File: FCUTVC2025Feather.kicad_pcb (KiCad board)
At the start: 2 copper layers, 60 x 131.5 mm, 53 parts, among them J1 Micro_SD_Card_Det2, J10 Conn_01x04, J11 Conn_01x04, J12 Conn_01x05, J13 Conn_01x05, J2 Conn_01x03, J3 Conn_01x03, J4 Conn_01x02, J5 Conn_01x02, J6 Conn_01x02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

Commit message: fixed drc
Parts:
- moved C30 0.20 mm to (131.2, 49.0)
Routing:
- net /MISO: track 50.2 -> 64.1 mm, vias 2 -> 3
- net +5V: track 81.2 -> 82.2 mm
- net /SCK: track 59.1 -> 58.5 mm, vias 5 -> 4
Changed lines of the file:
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@@
 	(footprint "Capacitor_SMD:C_0402_1005Metric"
 		(layer "B.Cu")
-		(at 131.2 48.8)
+		(at 131.2 49)
 		(descr "Capacitor SMD 0402 (1005 Metric), square (rectangular) end terminal, IPC_7351 nominal, (Body size source: IPC-SM-782 page 76, https://www.pcb-3d.com/wordpress/wp-content/uploads/ipc-sm-782a_amendment_1_and_2.pdf), generated with kicad-footprint-generator")
 		(tags "capacitor")
@@
 		)
 		(fp_line
-			(start -0.508 -2.8194)
-			(end -0.508 -2.7559)
-			(stroke
-				(width 0.1524)
-				(type solid)
-			)
-			(layer "B.CrtYd")
-		)
-		(fp_line
 			(start -0.508 -2.7559)
 			(end -2.4892 -2.7559)
@@
 		)
 		(fp_line
-			(start -0.508 2.7559)
-			(end -0.508 2.8194)
-			(stroke
-				(width 0.1524)
-				(type solid)
-			)
-			(layer "B.CrtYd")
-		)
-		(fp_line
-			(start -0.508 2.8194)
-			(end 0.508 2.8194)
-			(stroke
-				(width 0.1524)
-				(type solid)
-			)
-			(layer "B.CrtYd")
-		)
-		(fp_line
-			(start 0.508 -2.8194)
-			(end -0.508 -2.8194)
-			(stroke
-				(width 0.1524)
-				(type solid)
-			)
-			(layer "B.CrtYd")
-		)
-		(fp_line
-			(start 0.508 -2.7559)
-			(end 0.508 -2.8194)
-			(stroke
-				(width 0.1524)
-				(type solid)
-			)
-			(layer "B.CrtYd")
-		)
-		(fp_line
-			(start 0.508 2.8194)
-			(end 0.508 2.7559)
-			(stroke
-				(width 0.1524)
-				(type solid)
-			)
-			(layer "B.CrtYd")
-		)
-		(fp_line
-			(start 2.413508 -2.7204)
-			(end 2.4892 -2.723339)
-			(stroke
-				(width 0.1524)
-				(type solid)
-			)
-			(layer "B.CrtYd")
-		)
-		(fp_line
-			(start 2.4892 -2.7559)
-			(end 0.508 -2.7559)
+			(start -0.508 -2.7559)
+			(end 3.327908 -2.7559)
 			(stroke
 				(width 0.1524)
-				(type solid)
+				(type default)
 			)
 			(layer "B.CrtYd")
 		)
 		(fp_line
-			(start 2.4892 -2.723339)
-			(end 2.4892 -2.7559)
+			(start -0.508 2.7559)
+			(end 3.327908 2.7152)
 			(stroke
 				(width 0.1524)
-				(type solid)
+				(type default)
 			)
 			(layer "B.CrtYd")
@@
 	)
 	(via
-		(at 122.2 54.9)
+		(at 122.1 54.887952)
 		(size 0.6)
 		(drill 0.3)
@@
 	)
 	(via
-		(at 130.6 48.1)
+		(at 130.6 48.2)
 		(size 0.6)
 		(drill 0.3)
@@
 	)
 	(segment
+		(start 132.7 54.9)
+		(end 132.3 54.9)
+		(width 0.2)
+		(layer "F.Cu")
+		(net 5)
+	)
+	(segment
 		(start 123.2 59.8)
 		(end 123 60)
@@
 		(net 5)
 	)
+	(segment
+		(start 132.3 54.9)
+		(end 130.200555 56.999445)
+		(width 0.2)
+		(layer "F.Cu")
+		(net 5)
+	)
+	(segment
+		(start 130.200555 56.999445)
+		(end 124.074445 56.999445)
+		(width 0.2)
+		(layer "F.Cu")
+		(net 5)
+	)
+	(segment
+		(start 124.074445 56.999445)
+		(end 123.7 56.625)
+		(width 0.2)
+		(layer "F.Cu")
+		(net 5)
+	)
+	(via
+		(at 132.7 54.9)
+		(size 0.6)
+		(drill 0.3)
+		(layers "F.Cu" "B.Cu")
+		(net 5)
+	)
 	(via
 		(at 123.7 56.625)
@@
 	)
 	(segment
+		(start 133.01 54.59)
+		(end 133.01 51.1)
+		(width 0.2)
+		(layer "B.Cu")
+		(net 5)
+	)
+	(segment
 		(start 118.361865 58.6)
 		(end 117.2475 59.714365)
@@
 	)
 	(segment
+		(start 132.7 54.9)
+		(end 133.01 54.59)
+		(width 0.2)
+		(layer "B.Cu")
+		(net 5)
+	)
+	(segment
 		(start 133.975 59)
 		(end 123.045 69.93)
@@
 	)
 	(segment
+		(start 139.2675 39.3675)
+		(end 139.2675 49.61)
+		(width 0.4)
+		(layer "B.Cu")
+		(net 19)
+	)
+	(segment
+		(start 113 46.2)
+		(end 115.25 43.95)
+		(width 0.4)
+		(layer "B.Cu")
+		(net 19)
+	)
+	(segment
 		(start 102.75 66.675)
 		(end 101.75 66.675)
@@
 	)
 	(segment
-		(start 139.2675 41.061078)
-		(end 139.2675 49.61)
-		(width 0.4)
+		(start 101.75 66.675)
+		(end 101.65 66.575)
+		(width 0.2)
 		(layer "B.Cu")
 		(net 19)
 	)
 	(segment
-		(start 101.75 66.675)
-		(end 101.65 66.575)
-		(width 0.2)
+		(start 115.25 43.95)
+		(end 115.25 38.75)
+		(width 0.4)
 		(layer "B.Cu")
 		(net 19)
@@
 	)
 	(segment
-		(start 115.25 38.75)
-		(end 116.25 37.75)
-		(width 0.4)
-		(layer "B.Cu")
-		(net 19)
-	)
-	(segment
-		(start 135.956422 37.75)
-		(end 139.2675 41.061078)
-		(width 0.4)
-		(layer "B.Cu")
-		(net 19)
-	)
-	(segment
-		(start 116.25 37.75)
-		(end 135.956422 37.75)
+		(start 137.65 37.75)
+		(end 139.2675 39.3675)
 		(width 0.4)
 		(layer "B.Cu")
@@
 	)
 	(segment
-		(start 115.25 43.95)
-		(end 115.25 38.75)
-		(width 0.4)
-		(layer "B.Cu")
-		(net 19)
-	)
-	(segment
-		(start 113 46.2)
-		(end 115.25 43.95)
+		(start 115.25 38.75)
+		(end 116.25 37.75)
 		(width 0.4)
 		(layer "B.Cu")
@@
 	)
 	(segment
+		(start 116.25 37.75)
+		(end 137.65 37.75)
+		(width 0.4)
+		(layer "B.Cu")
+		(net 19)
+	)
+	(segment
 		(start 140.95 133.7)
 		(end 140.95 133.63)
@@
 	)
 	(segment
-		(start 121.7 57.6)
-		(end 121.7 54.9025)
+		(start 121.5 57.4)
+		(end 121.5 54.7025)
 		(width 0.2)
 		(layer "B.Cu")
@@
 	(segment
 		(start 121.975 57.875)
-		(end 121.7 57.6)
+		(end 121.5 57.4)
 		(width 0.2)
 		(layer "B.Cu")
@@
 	)
 	(segment
-		(start 127.075 57.875)
-		(end 124.925 57.875)
+		(start 121.5 54.7025)
+		(end 118.9475 52.15)
 		(width 0.2)
 		(layer "B.Cu")
@@
 	)
 	(segment
-		(start 121.7 54.9025)
-		(end 118.9475 52.15)
+		(start 127.075 57.875)
+		(end 124.925 57.875)
 		(width 0.2)
 		(layer "B.Cu")
@@
 	)
 	(via
-		(at 123 55)
-		(size 0.6)
-		(drill 0.3)
-		(layers "F.Cu" "B.Cu")
-		(net 27)
-	)
-	(via
 		(at 127 52)
 		(size 0.6)
@@
 	)
 	(segment
-		(start 123.875 54.125)
-		(end 123 55)
+		(start 115.8 53.541865)
+		(end 118.341865 51)
 		(width 0.2)
 		(layer "B.Cu")
@@
 	)
 	(segment
-		(start 131.51 49.5)
-		(end 131.155 49.145)
+		(start 132.429179 50.255692)
+		(end 132.429179 48.714179)
 		(width 0.2)
 		(layer "B.Cu")
@@
 	)
 	(segment
-		(start 124.925 54.125)
-		(end 124.925 54.075)
+		(start 120.75 51)
+		(end 123.875 54.125)
 		(width 0.2)
 		(layer "B.Cu")
@@
 	)
 	(segment
-		(start 116.5 65.1)
-		(end 115.8 64.4)
+		(start 123.875 54.125)
+		(end 124.925 54.125)
 		(width 0.2)
 		(layer "B.Cu")
@@
 	)
 	(segment
-		(start 120.203135 51.05)
-		(end 123 53.846865)
+		(start 131.155 47.44)
+		(end 131.155 47.09)
 		(width 0.2)
 		(layer "B.Cu")
@@
 	)
 	(segment
-		(start 123.475432 65.2)
-		(end 126 62.675432)
+		(start 124.925 54.125)
+		(end 124.925 54.075)
 		(width 0.2)
 		(layer "B.Cu")
@@
 	)
 	(segment
-		(start 131.51 49.9)
-		(end 131.51 49.5)
+		(start 116.5 65.1)
+		(end 115.8 64.4)
 		(width 0.2)
 		(layer "B.Cu")
@@
 	)
 	(segment
-		(start 123 53.846865)
-		(end 123 55)
+		(start 123.475432 65.2)
+		(end 126 62.675432)
 		(width 0.2)
 		(layer "B.Cu")
@@
 	)
 	(segment
-		(start 118.291865 51.05)
-		(end 120.203135 51.05)
-		(width 0.2)
-		(layer "B.Cu")
-		(net 27)
-	)
-	(segment
 		(start 126 62.675432)
 		(end 126 62.33)
@@
 	)
 	(segment
-		(start 115.8 64.4)
-		(end 115.8 53.541865)
+		(start 118.341865 51)
+		(end 120.75 51)
 		(width 0.2)
 		(layer "B.Cu")
@@
 	)
 	(segment
-		(start 124.925 54.125)
-		(end 123.875 54.125)
-		(width 0.2)
-		(layer "B.Cu")
-		(net 27)
-	)
-	(segment
 		(start 132.073487 49.9)
 		(end 132.429179 50.255692)
@@
 	)
 	(segment
-		(start 131.155 47.09)
-		(end 131.155 49.145)
+		(start 131.51 49.9)
+		(end 132.073487 49.9)
 		(width 0.2)
 		(layer "B.Cu")
@@
 	)
 	(segment
-		(start 131.51 49.9)
-		(end 132.073487 49.9)
+		(start 132.429179 48.714179)
+		(end 131.155 47.44)
 		(width 0.2)
 		(layer "B.Cu")
@@
 	)
 	(segment
-		(start 115.8 53.541865)
-		(end 118.291865 51.05)
+		(start 115.8 64.4)
+		(end 115.8 53.541865)
 		(width 0.2)
 		(layer "B.Cu")

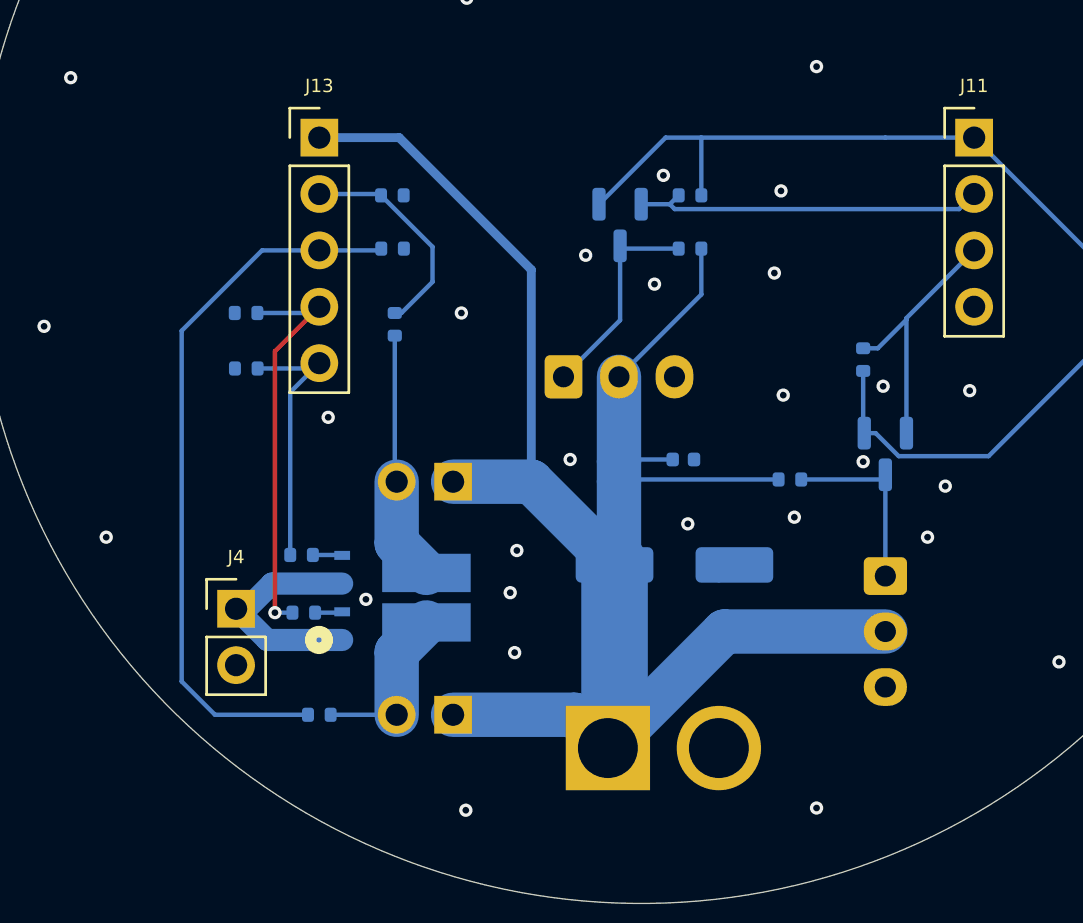
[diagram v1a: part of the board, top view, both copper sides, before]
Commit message: changed servo and pyro headers to JST XH (w/ hole). V1 complete
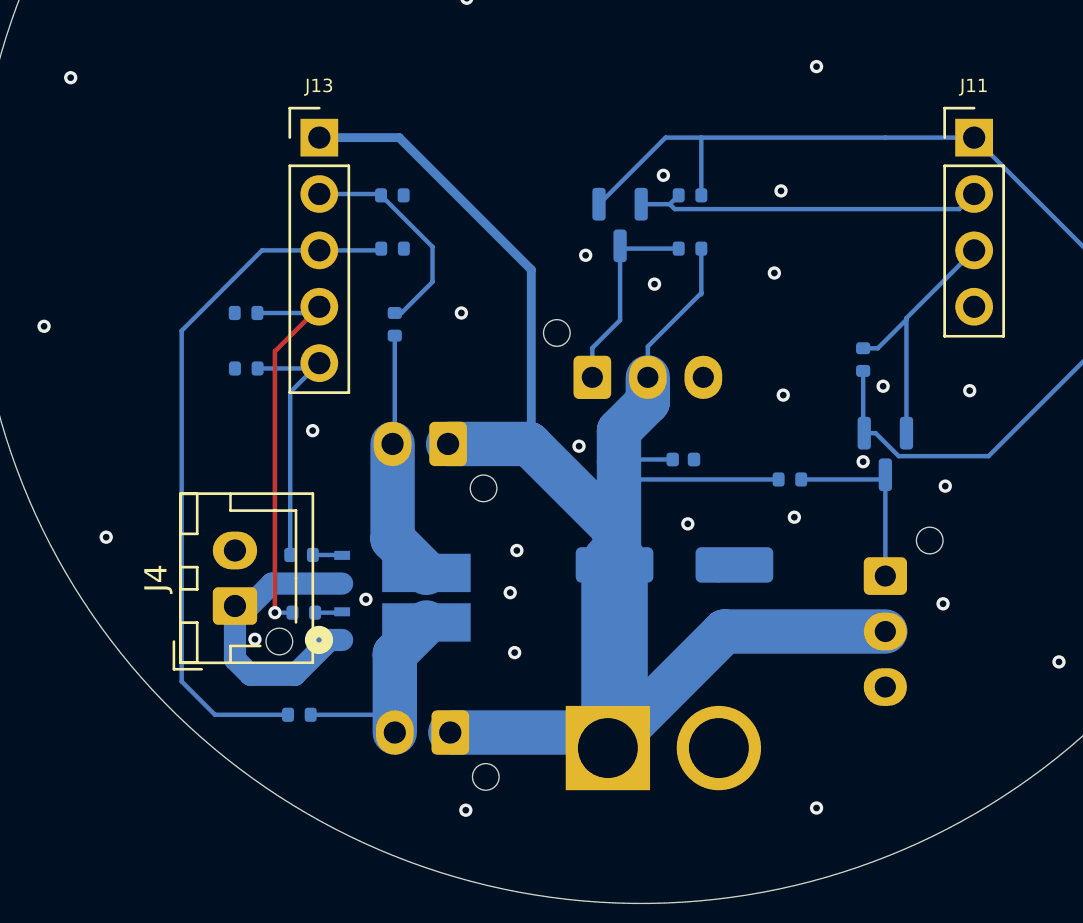
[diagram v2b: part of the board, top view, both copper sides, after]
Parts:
- J2, J3: footprint Connector_JST:JST_XH_B3B-XH-A_1x03_P2.50mm_Vertical -> Connector_JST:JST_XH_B3B-XH-AM_1x03_P2.50mm_Vertical
- J4, J6, J8: footprint Connector_PinHeader_2.54mm:PinHeader_1x02_P2.54mm_Vertical -> Connector_JST:JST_XH_B2B-XH-AM_1x02_P2.50mm_Vertical
- moved J8 1.71 mm to (120.3, 139.3), turned to 180 degrees
- moved J2 1.30 mm to (126.8, 136.3)
- moved R16 0.90 mm to (113.6, 151.5)
- moved J6 0.81 mm to (120.4, 152.3), turned to 180 degrees
- moved J4 0.13 mm to (110.7, 146.6), turned to 90 degrees
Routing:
- net Net-(J4-Pin_1): track 10.6 -> 13.4 mm
- net /PYO1: track 7.69 -> 9.42 mm
- net +6V/+8V: track 86.2 -> 87.2 mm
- net /PYC1: track 32.6 -> 31.7 mm
- net /SRV1O: track 9.65 -> 9.13 mm
- net GND: vias 98 -> 99

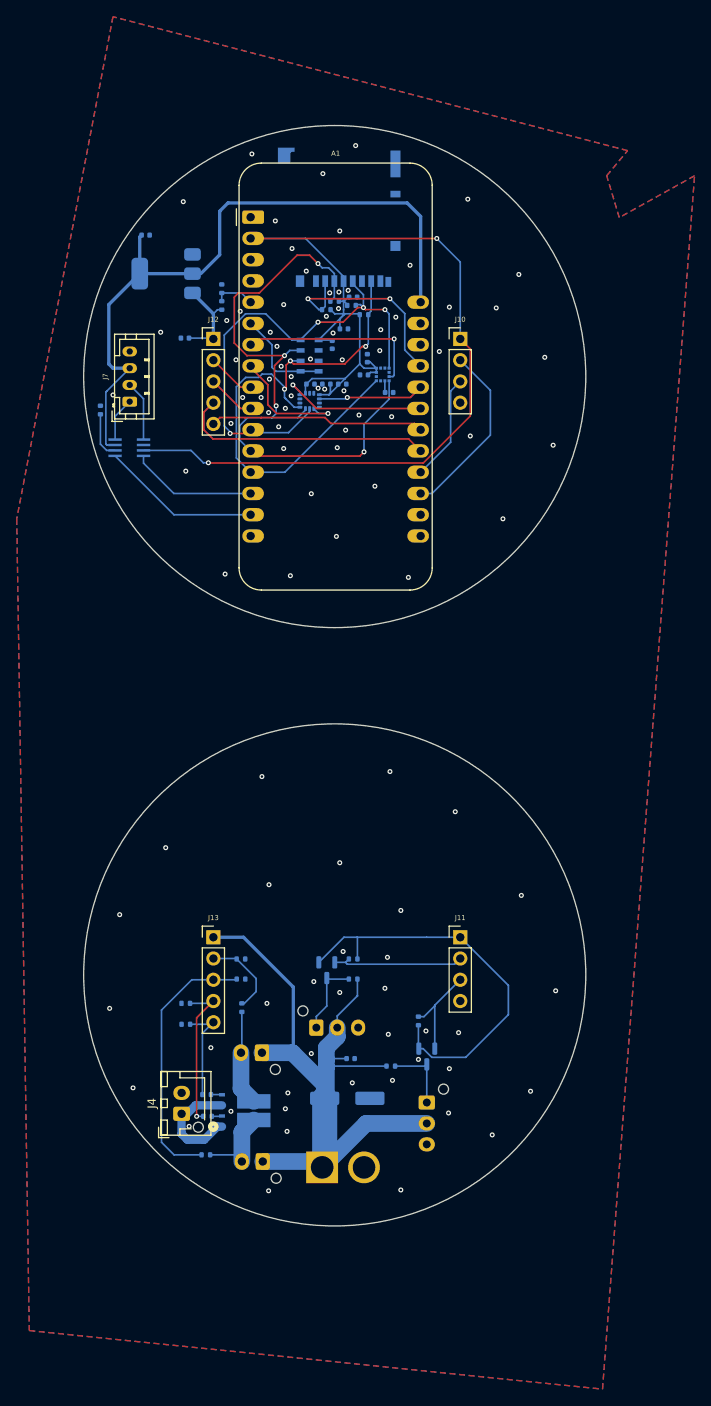
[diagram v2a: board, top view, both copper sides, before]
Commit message: added mounting holes (25mm 0 degrees, 150 degrees, 210 degrees)
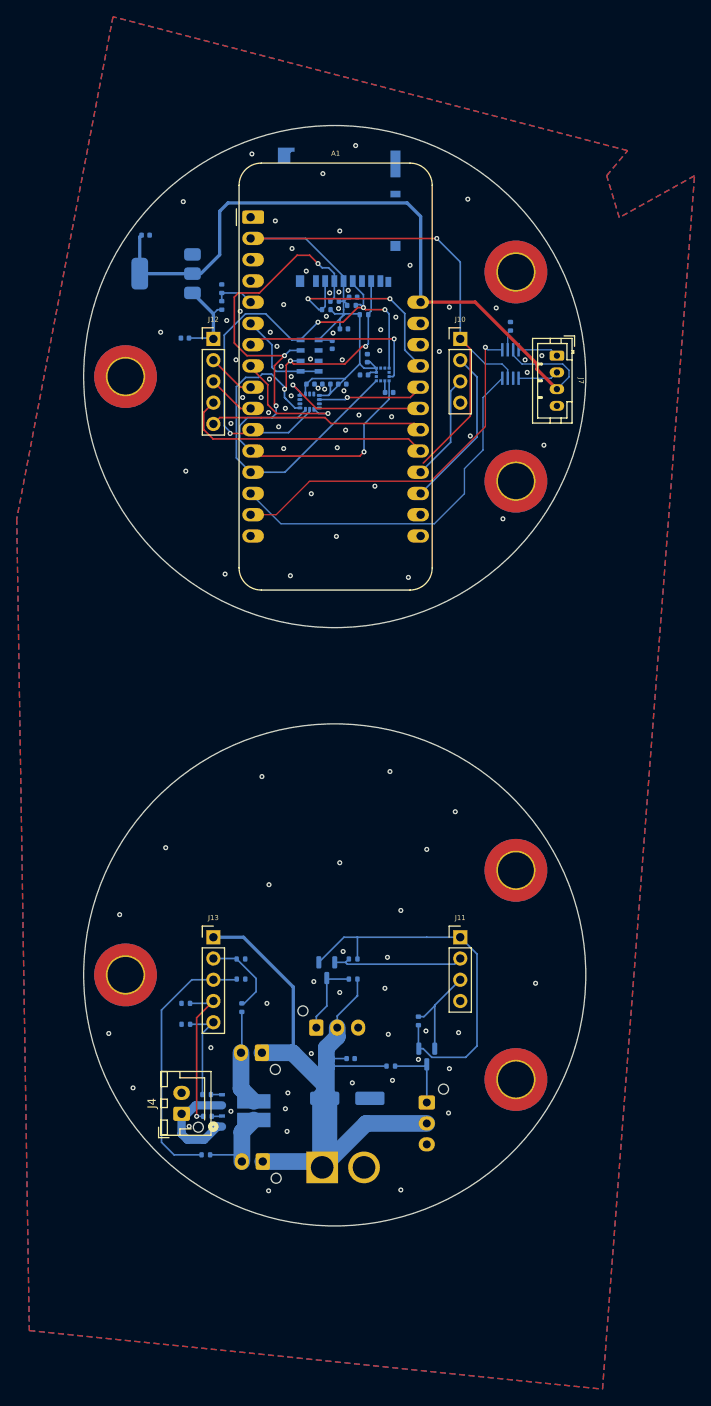
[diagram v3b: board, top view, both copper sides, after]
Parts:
- added H1: MountingHole_Pad, MountingHole:MountingHole_4.3mm_M4_DIN965_Pad_TopBottom, F.Cu at (104.0, 58.5)
- added H2: MountingHole_Pad, MountingHole:MountingHole_4.3mm_M4_DIN965_Pad_TopBottom, F.Cu at (150.7, 71.0)
- added H3: MountingHole_Pad, MountingHole:MountingHole_4.3mm_M4_DIN965_Pad_TopBottom, F.Cu at (150.7, 46.0)
- added H4: MountingHole_Pad, MountingHole:MountingHole_4.3mm_M4_DIN965_Pad_TopBottom, F.Cu at (104.0, 130.0)
- added H5: MountingHole_Pad, MountingHole:MountingHole_4.3mm_M4_DIN965_Pad_TopBottom, F.Cu at (150.7, 117.5)
- added H6: MountingHole_Pad, MountingHole:MountingHole_4.3mm_M4_DIN965_Pad_TopBottom, F.Cu at (150.7, 142.5)
- moved J7 51.3 mm to (155.6, 56.0), turned to -90 degrees
- moved R17 50.0 mm to (150.0, 52.5)
- moved U1 46.6 mm to (150.0, 57.0), turned to 90 degrees
- moved U4 0.09 mm to (126.0, 61.5)
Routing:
- net /UART0_RX: track 15.2 -> 44.2 mm
- net +3V3: track 143.3 -> 117.5 mm, vias 2 -> 1
- net /UART0_TX: track 19.1 -> 44.0 mm, vias 0 -> 1
- net +5V: track 82.2 -> 87.6 mm
- net /UART_EN: track 5.63 -> 2.43 mm
- net +3V3B: track 48.4 -> 45.3 mm
- net /RX0: track 7.21 -> 4.86 mm
- net /SRV1A: track 21.7 -> 19.5 mm
- net GND: vias 99 -> 97

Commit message: Added cut for wire routing and changed a pyro channel to facing up
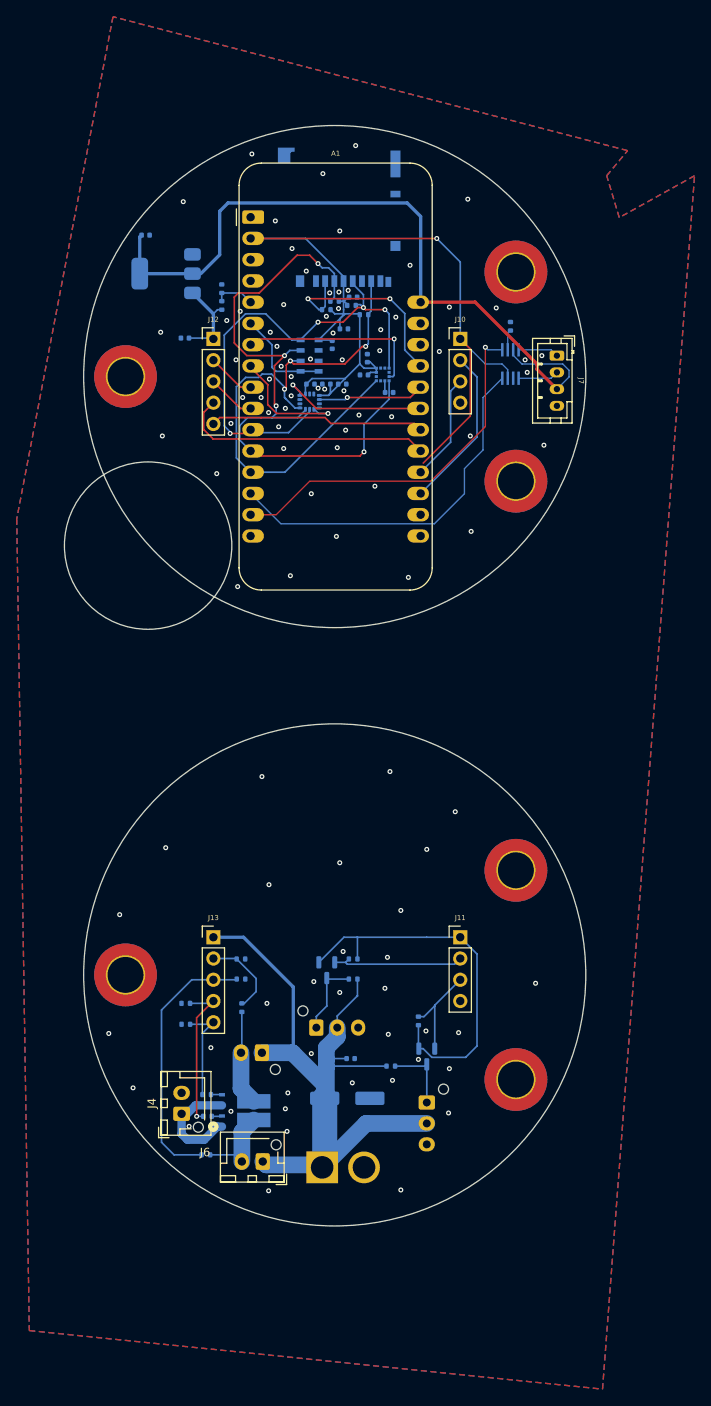
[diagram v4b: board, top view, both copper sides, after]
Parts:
- J6: moved to F.Cu
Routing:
- net +6V/+8V: track 87.2 -> 87.7 mm
- net GND: vias 97 -> 98
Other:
- board size 60 x 131.5 mm -> 62.3 x 131.5 mm
